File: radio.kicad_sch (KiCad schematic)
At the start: 16 parts, among them U8 Si4468/7, Y2 30MHz

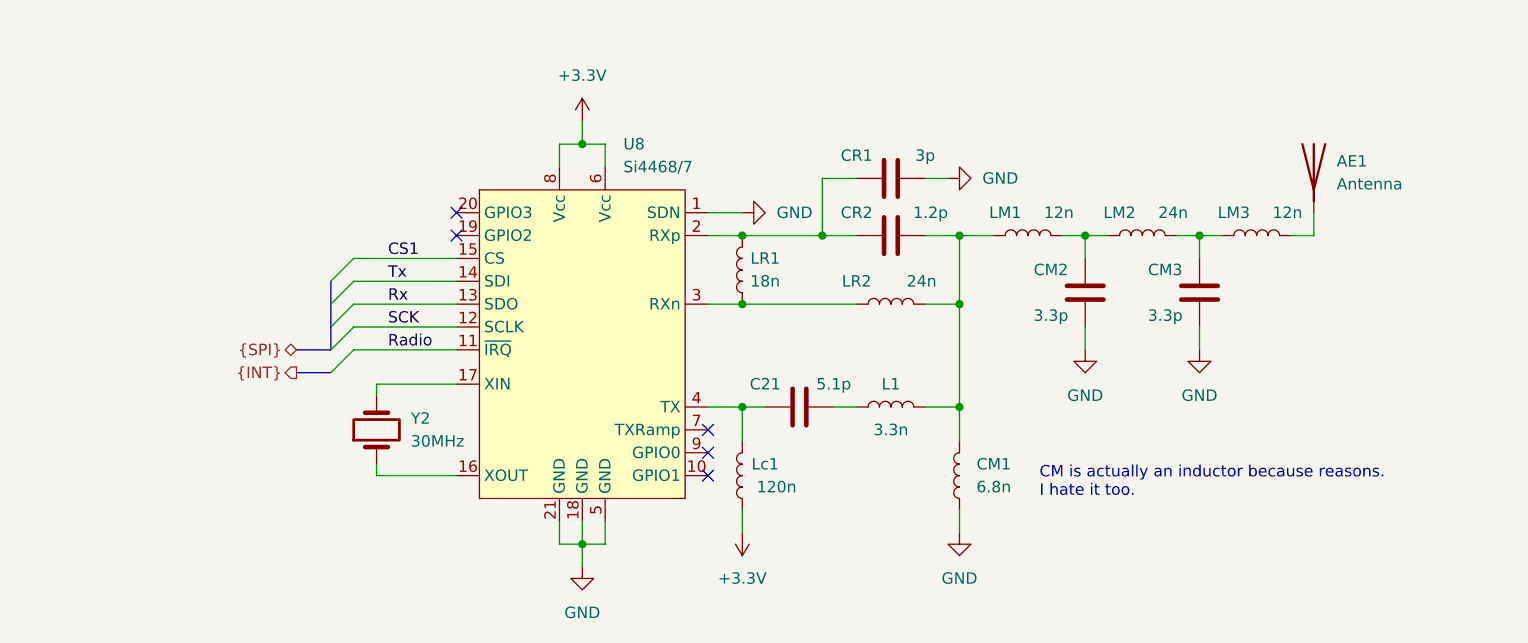
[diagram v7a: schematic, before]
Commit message: Centered RP2040, added mounting hardware, Rearranged radio
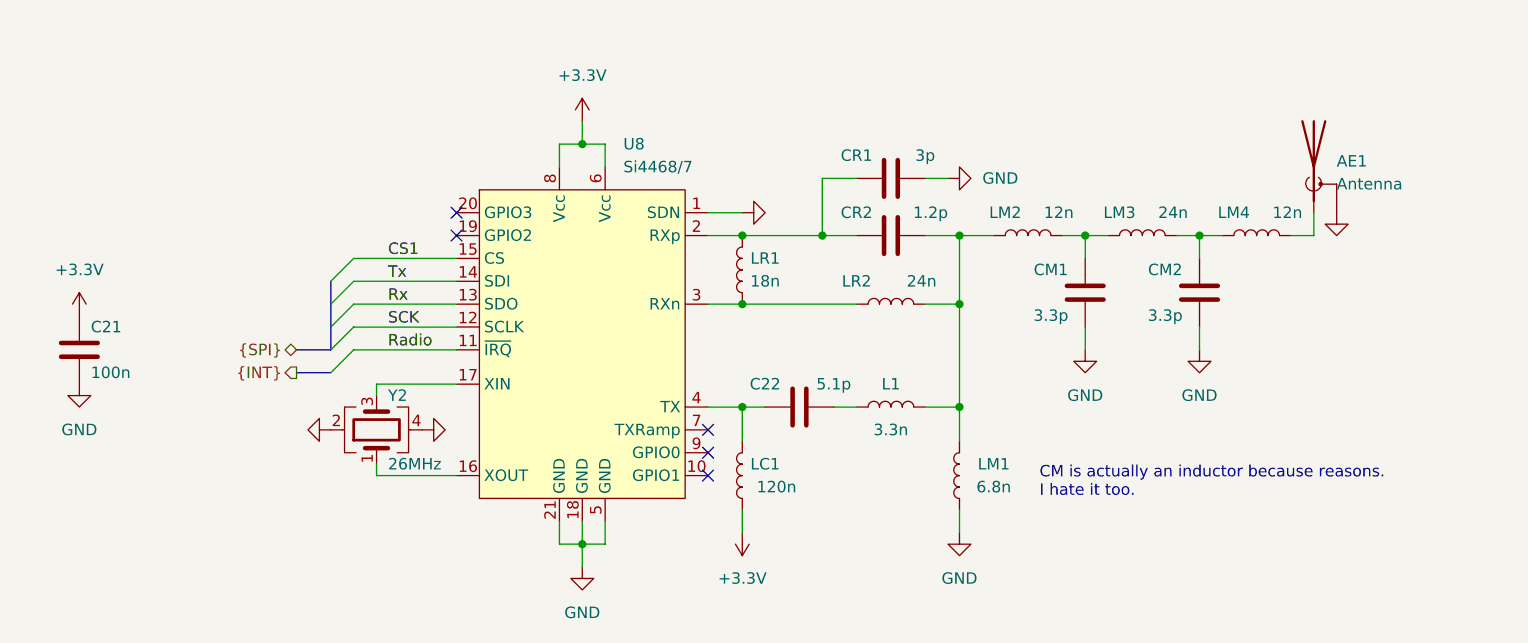
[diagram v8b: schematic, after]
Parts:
- added C21: 100n, Capacitor_SMD:C_0603_1608Metric, symbol Device:C
- AE1: symbol Device:Antenna -> Device:Antenna_Shield
- Y2: value 30MHz -> 26MHz; symbol Device:Crystal -> Device:Crystal_GND24
- renumbered C21 to C22, CM2 to CM1, CM3 to CM2, Lc1 to LC1, CM1 to LM1, LM1 to LM2, LM2 to LM3, LM3 to LM4
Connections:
- net +3V3: now also C21.1
- net GND: now also AE1.2 (Shield), Y2.2, Y2.4, C21.2
- net at U8.17 (XIN): now also Y2.3; no longer Y2.2
